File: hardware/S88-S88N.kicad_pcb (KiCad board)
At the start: 2 copper layers, 27.1 x 23.1 mm, 4 parts, among them J1 RJ45, P1 CONN_6, P2 CONN_6

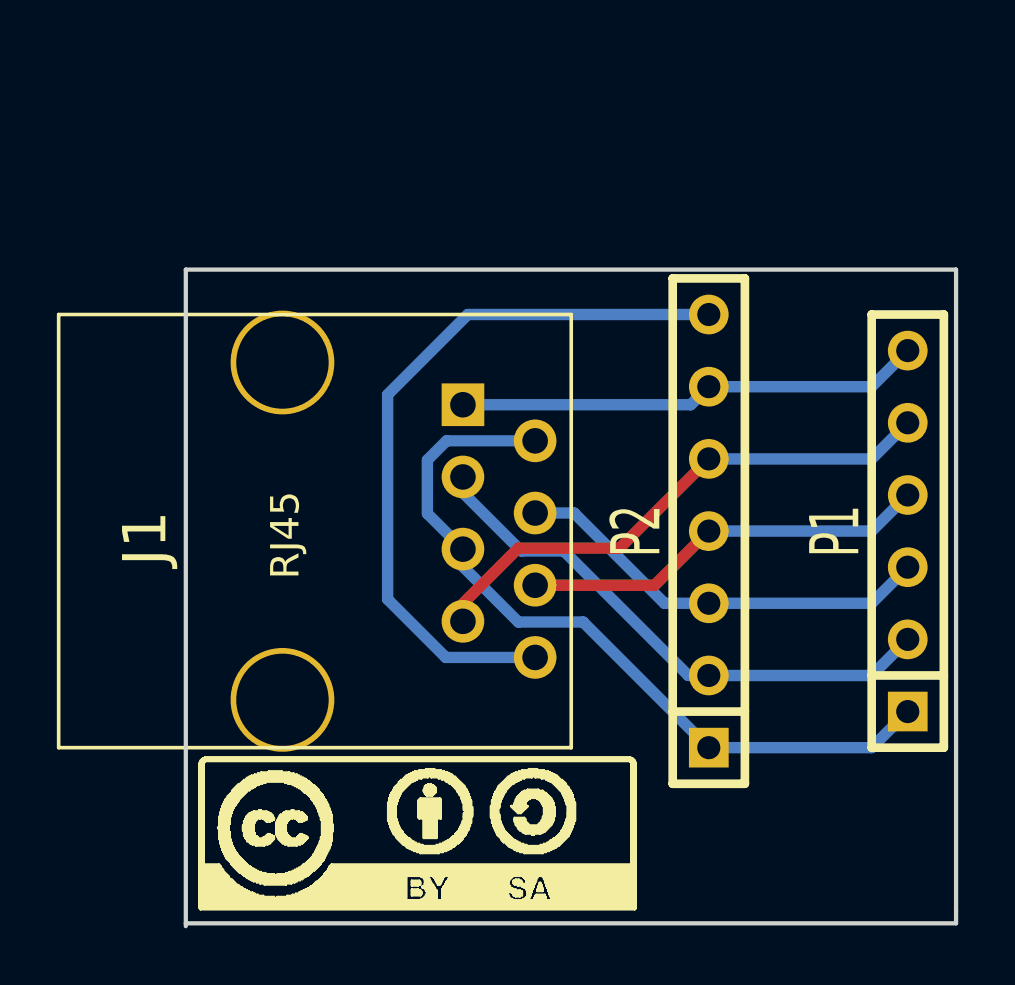
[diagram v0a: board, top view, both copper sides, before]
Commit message: Updated Silkscreen
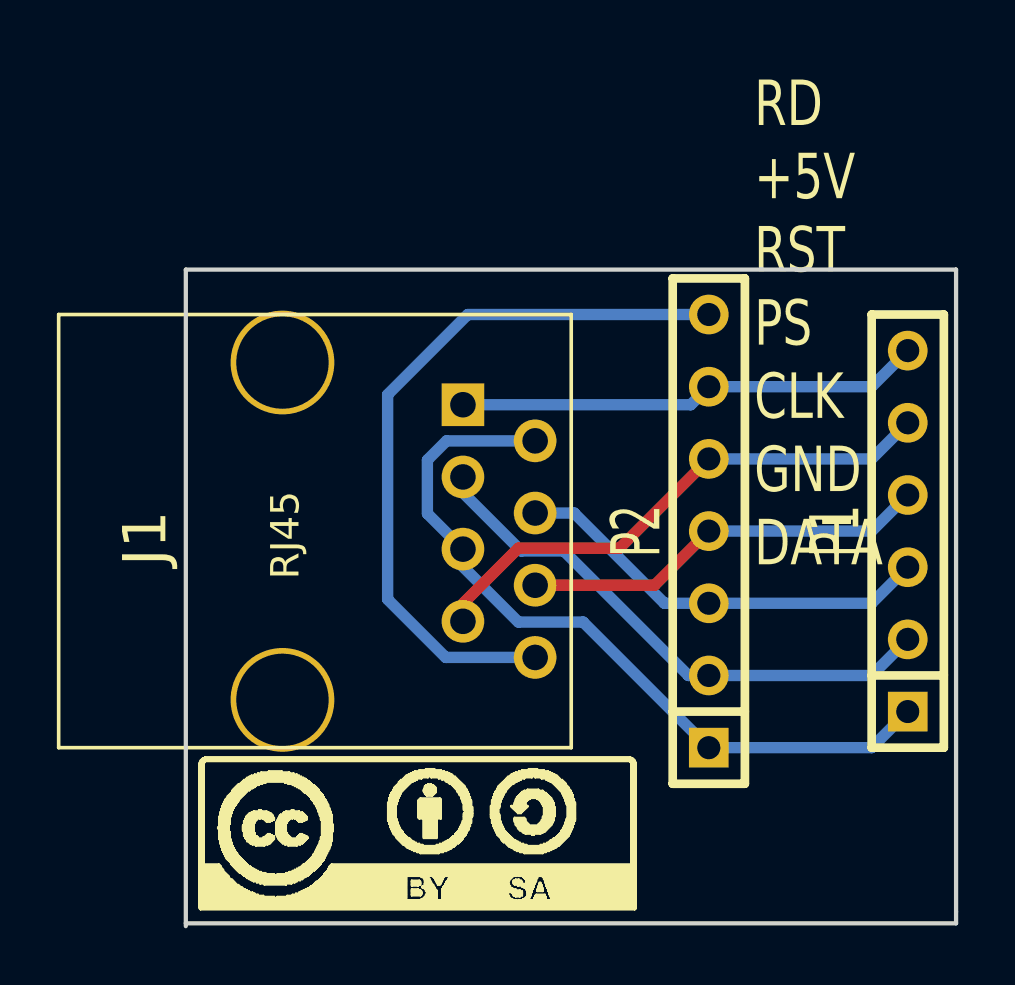
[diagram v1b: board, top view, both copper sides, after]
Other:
- board text added: "Board by Dirkjan Krijnders github.com/dirkjankrijnders/S88NAVR"
- board text added: "RD +5V RST PS CLK GND DATA"
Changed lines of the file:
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@@
     (links 14)
     (no_connects 0)
-    (area 0 0 0 0)
+    (area 89.524999 73.724999 116.775001 96.975001)
     (thickness 1.6)
-    (drawings 5)
+    (drawings 7)
     (tracks 41)
     (zones 0)
@@
     (visible_elements FFFFF7BF)
     (pcbplotparams
-      (layerselection 3178497)
+      (layerselection 284196865)
       (usegerberextensions true)
       (excludeedgelayer true)
@@
       (outputformat 1)
       (mirror false)
-      (drillshape 1)
+      (drillshape 0)
       (scaleselection 1)
-      (outputdirectory ""))
+      (outputdirectory "Outputs/Rev. 0/"))
   )
   (net 0 "")
@@
     (fp_line (start 0.17018 -5.31368) (end 0.17018 -5.35178) (layer F.SilkS) (width 0.06604))
   )
+  (gr_text "Board by Dirkjan Krijnders\ngithub.com/dirkjankrijnders/S88NAVR\n" (at 115.1 93.9) (layer B.SilkS)
+    (effects (font (size 0.8 0.8) (thickness 0.2)) (justify left mirror))
+  )
+  (gr_text "RD\n+5V\nRST\nPS\nCLK\nGND\nDATA" (at 109.6 75.7) (layer F.SilkS)
+    (effects (font (size 1.6 1.2) (thickness 0.25)) (justify left))
+  )
   (gr_line (start 116.7 96.8) (end 89.6 96.8) (angle 90) (layer Edge.Cuts) (width 0.15))

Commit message: Fixed short between GND and Data
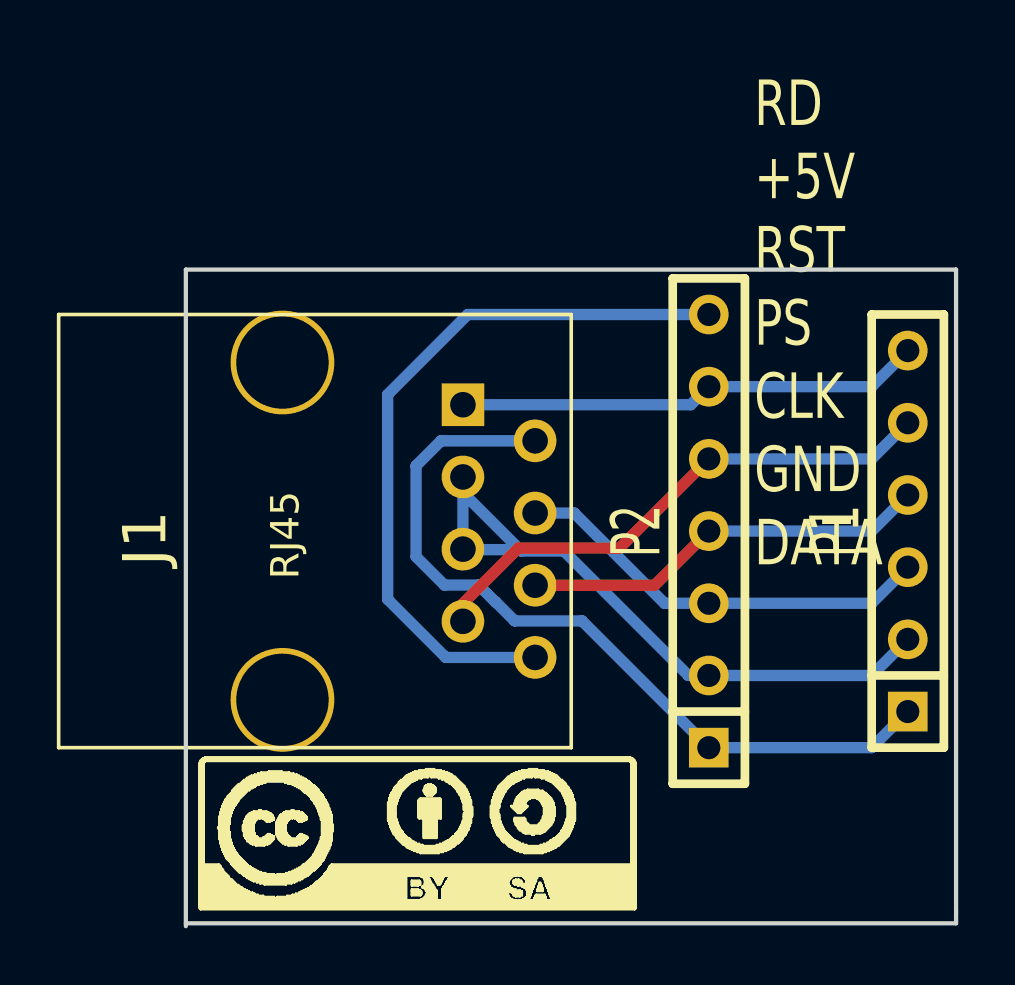
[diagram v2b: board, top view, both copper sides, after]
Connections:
- J1 pad 2: N-000007 -> N-000006
- J1 pad 3: N-000008 (its old number) -> N-000007
- P1 pad 1: N-000007 -> N-000006
- P1 pad 2: N-000008 (its old number) -> N-000007
- P2 pad 1: N-000007 -> N-000006
- P2 pad 2: N-000008 (its old number) -> N-000007
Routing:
- net N-000006: track 0.00 -> 28.4 mm
- net N-000008 (its old number): track 19.4 -> 0.00 mm
- net N-000007: track 27.2 -> 23.9 mm
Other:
- net class Default: trace_width 0.4 -> 0.39878
